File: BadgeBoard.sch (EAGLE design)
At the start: 15 parts

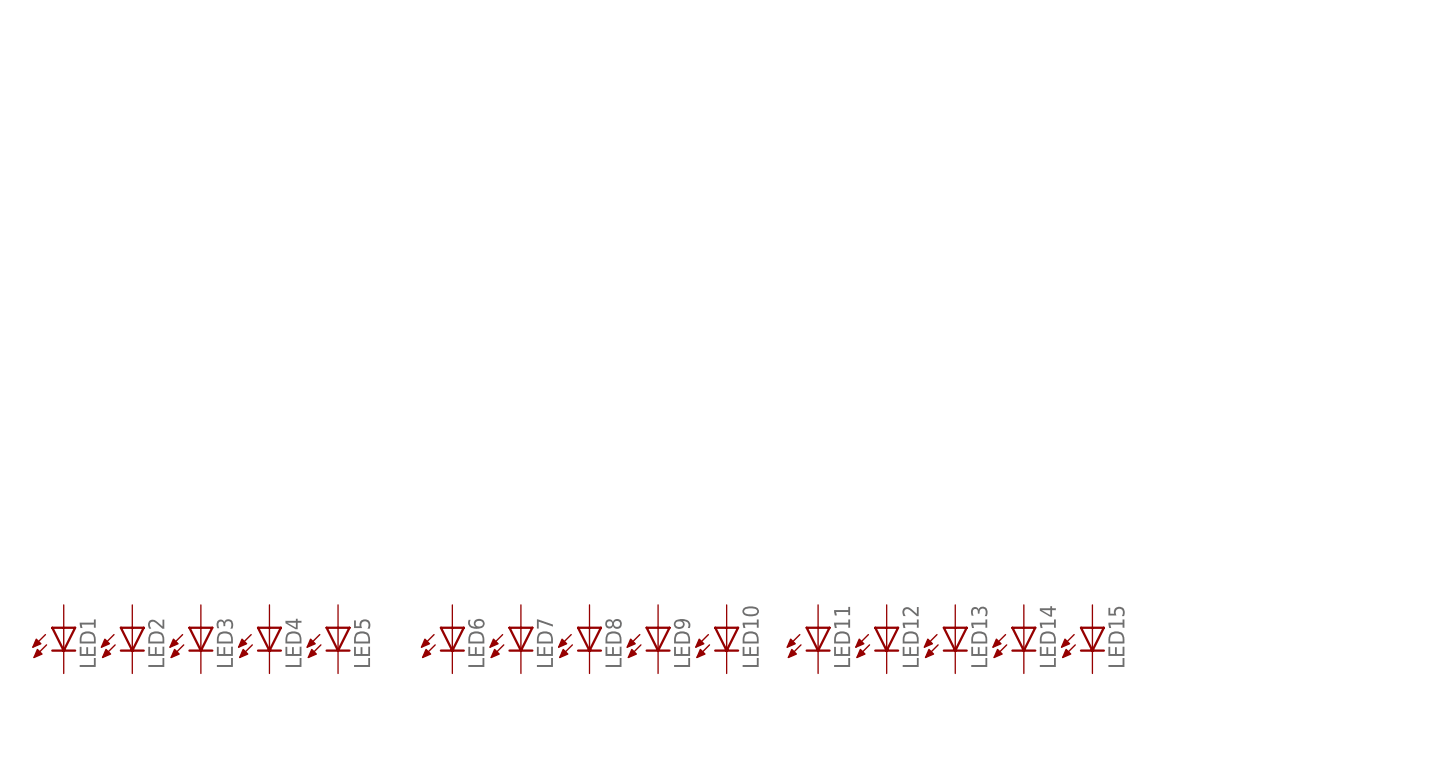
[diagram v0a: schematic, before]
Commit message: update led matrix
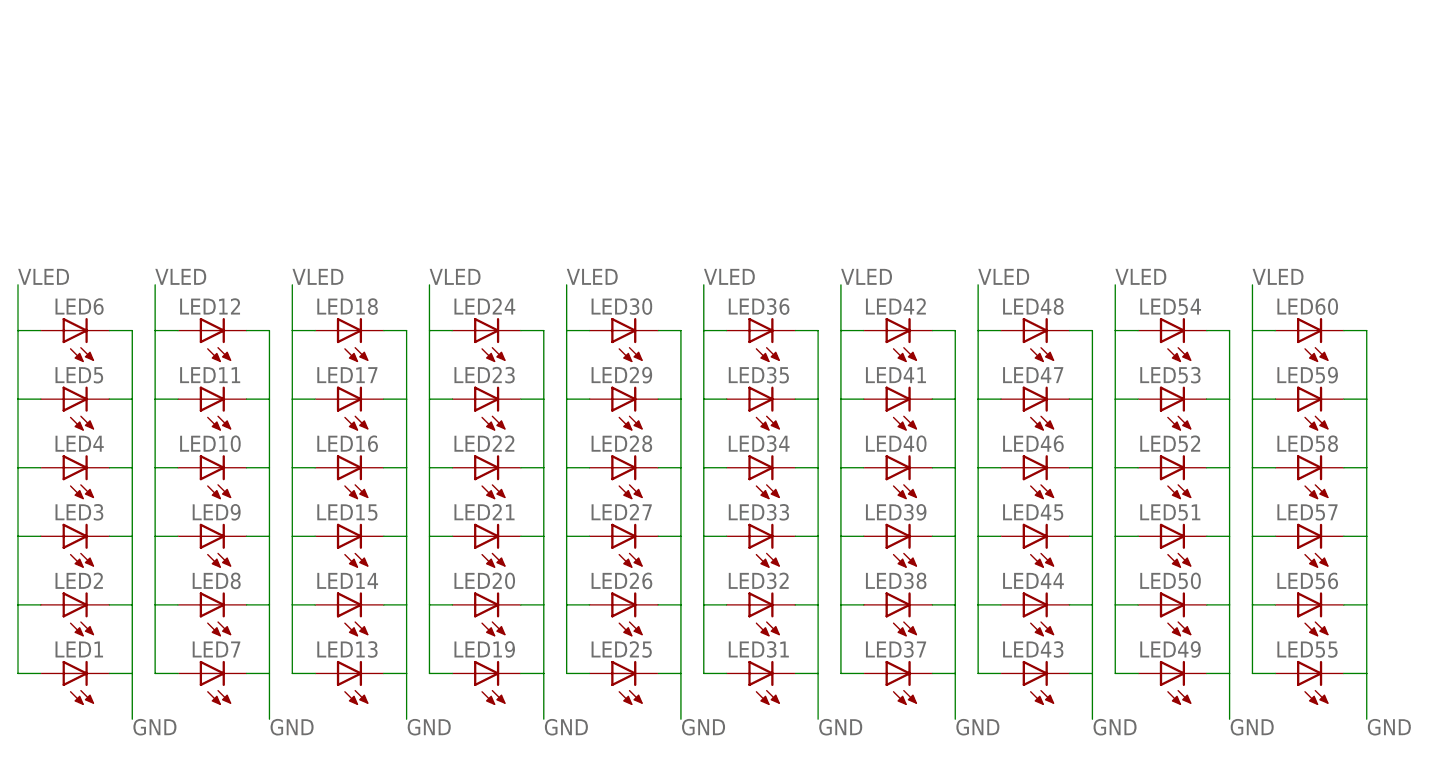
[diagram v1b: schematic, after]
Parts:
- added LED16, LED17, LED18, LED19, LED20, LED21, LED22, LED23, LED24, LED25, LED26, LED27, LED28, LED29, LED30, LED31, LED32, LED33, LED34, LED35, LED36, LED37, LED38, LED39, LED40, LED41, LED42, LED43, LED44, LED45, LED46, LED47, LED48, LED49, LED50, LED51, LED52, LED53, LED54, LED55, LED56, LED57, LED58, LED59, LED60: (no value), adafruit:LED3MM
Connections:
- new net GND: LED10.C, LED11.C, LED12.C, LED7.C, LED8.C, LED9.C
- new net VLED: LED10.A, LED11.A, LED12.A, LED7.A, LED8.A, LED9.A
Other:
- moved on the sheet: LED1, LED10, LED11, LED12, LED13, LED14, LED15, LED2, LED3, LED4, LED5, LED6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

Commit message: More layout
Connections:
- net GND: now also LED1.C, LED13.C, LED14.C, LED15.C, LED16.C, LED17.C, LED18.C, LED19.C, LED2.C, LED20.C, LED21.C, LED22.C, LED23.C, LED24.C, LED25.C, LED26.C, LED27.C, LED28.C, LED29.C, LED3.C, LED30.C, LED31.C, LED32.C, LED33.C, LED34.C, LED35.C, LED36.C, LED37.C, LED38.C, LED39.C, LED4.C, LED40.C, LED41.C, LED42.C, LED43.C, LED44.C, LED45.C, LED46.C, LED47.C, LED48.C, LED49.C, LED5.C, LED50.C, LED51.C, LED52.C, LED53.C, LED54.C, LED55.C, LED56.C, LED57.C, LED58.C, LED59.C, LED6.C, LED60.C
- net VLED: now also LED1.A, LED13.A, LED14.A, LED15.A, LED16.A, LED17.A, LED18.A, LED19.A, LED2.A, LED20.A, LED21.A, LED22.A, LED23.A, LED24.A, LED25.A, LED26.A, LED27.A, LED28.A, LED29.A, LED3.A, LED30.A, LED31.A, LED32.A, LED33.A, LED34.A, LED35.A, LED36.A, LED37.A, LED38.A, LED39.A, LED4.A, LED40.A, LED41.A, LED42.A, LED43.A, LED44.A, LED45.A, LED46.A, LED47.A, LED48.A, LED49.A, LED5.A, LED50.A, LED51.A, LED52.A, LED53.A, LED54.A, LED55.A, LED56.A, LED57.A, LED58.A, LED59.A, LED6.A, LED60.A
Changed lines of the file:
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@@
 <setting verticaltext="up"/>
 </settings>
-<grid distance="0.1" unitdist="inch" unit="inch" style="lines" multiple="1" display="yes" altdistance="0.01" altunitdist="inch" altunit="inch"/>
+<grid distance="0.1" unitdist="inch" unit="inch" style="lines" multiple="1" display="no" altdistance="0.01" altunitdist="inch" altunit="inch"/>
 <layers>
 <layer number="1" name="Top" color="4" fill="1" visible="no" active="no"/>
@@
 <wire x1="2.54" y1="20.32" x2="5.08" y2="20.32" width="0.1524" layer="91"/>
 <wire x1="2.54" y1="12.7" x2="5.08" y2="12.7" width="0.1524" layer="91"/>
+<pinref part="LED6" gate="G$1" pin="A"/>
+<pinref part="LED5" gate="G$1" pin="A"/>
+<pinref part="LED4" gate="G$1" pin="A"/>
+<pinref part="LED3" gate="G$1" pin="A"/>
+<pinref part="LED2" gate="G$1" pin="A"/>
+<pinref part="LED1" gate="G$1" pin="A"/>
 </segment>
 <segment>
@@
 <wire x1="33.02" y1="20.32" x2="35.56" y2="20.32" width="0.1524" layer="91"/>
 <wire x1="33.02" y1="12.7" x2="35.56" y2="12.7" width="0.1524" layer="91"/>
+<pinref part="LED18" gate="G$1" pin="A"/>
+<pinref part="LED17" gate="G$1" pin="A"/>
+<pinref part="LED16" gate="G$1" pin="A"/>
+<pinref part="LED15" gate="G$1" pin="A"/>
+<pinref part="LED14" gate="G$1" pin="A"/>
+<pinref part="LED13" gate="G$1" pin="A"/>
 </segment>
 <segment>
@@
 <wire x1="48.26" y1="20.32" x2="50.8" y2="20.32" width="0.1524" layer="91"/>
 <wire x1="48.26" y1="12.7" x2="50.8" y2="12.7" width="0.1524" layer="91"/>
+<pinref part="LED19" gate="G$1" pin="A"/>
+<pinref part="LED20" gate="G$1" pin="A"/>
+<pinref part="LED21" gate="G$1" pin="A"/>
+<pinref part="LED22" gate="G$1" pin="A"/>
+<pinref part="LED23" gate="G$1" pin="A"/>
+<pinref part="LED24" gate="G$1" pin="A"/>
 </segment>
 <segment>
@@
 <wire x1="63.5" y1="20.32" x2="66.04" y2="20.32" width="0.1524" layer="91"/>
 <wire x1="63.5" y1="12.7" x2="66.04" y2="12.7" width="0.1524" layer="91"/>
+<pinref part="LED30" gate="G$1" pin="A"/>
+<pinref part="LED29" gate="G$1" pin="A"/>
+<pinref part="LED28" gate="G$1" pin="A"/>
+<pinref part="LED27" gate="G$1" pin="A"/>
+<pinref part="LED26" gate="G$1" pin="A"/>
+<pinref part="LED25" gate="G$1" pin="A"/>
 </segment>
 <segment>
@@
 <wire x1="78.74" y1="20.32" x2="81.28" y2="20.32" width="0.1524" layer="91"/>
 <wire x1="78.74" y1="12.7" x2="81.28" y2="12.7" width="0.1524" layer="91"/>
+<pinref part="LED31" gate="G$1" pin="A"/>
+<pinref part="LED32" gate="G$1" pin="A"/>
+<pinref part="LED33" gate="G$1" pin="A"/>
+<pinref part="LED34" gate="G$1" pin="A"/>
+<pinref part="LED35" gate="G$1" pin="A"/>
+<pinref part="LED36" gate="G$1" pin="A"/>
 </segment>
 <segment>
@@
 <wire x1="109.22" y1="20.32" x2="111.76" y2="20.32" width="0.1524" layer="91"/>
 <wire x1="109.22" y1="12.7" x2="111.76" y2="12.7" width="0.1524" layer="91"/>
+<pinref part="LED43" gate="G$1" pin="A"/>
+<pinref part="LED44" gate="G$1" pin="A"/>
+<pinref part="LED45" gate="G$1" pin="A"/>
+<pinref part="LED46" gate="G$1" pin="A"/>
+<pinref part="LED47" gate="G$1" pin="A"/>
+<pinref part="LED48" gate="G$1" pin="A"/>
 </segment>
 <segment>
@@
 <wire x1="93.98" y1="20.32" x2="96.52" y2="20.32" width="0.1524" layer="91"/>
 <wire x1="93.98" y1="12.7" x2="96.52" y2="12.7" width="0.1524" layer="91"/>
+<pinref part="LED42" gate="G$1" pin="A"/>
+<pinref part="LED41" gate="G$1" pin="A"/>
+<pinref part="LED40" gate="G$1" pin="A"/>
+<pinref part="LED39" gate="G$1" pin="A"/>
+<pinref part="LED38" gate="G$1" pin="A"/>
+<pinref part="LED37" gate="G$1" pin="A"/>
 </segment>
 <segment>
@@
 <wire x1="124.46" y1="20.32" x2="127" y2="20.32" width="0.1524" layer="91"/>
 <wire x1="124.46" y1="12.7" x2="127" y2="12.7" width="0.1524" layer="91"/>
+<pinref part="LED54" gate="G$1" pin="A"/>
+<pinref part="LED53" gate="G$1" pin="A"/>
+<pinref part="LED52" gate="G$1" pin="A"/>
+<pinref part="LED51" gate="G$1" pin="A"/>
+<pinref part="LED50" gate="G$1" pin="A"/>
+<pinref part="LED49" gate="G$1" pin="A"/>
 </segment>
 <segment>
@@
 <wire x1="139.7" y1="20.32" x2="142.24" y2="20.32" width="0.1524" layer="91"/>
 <wire x1="139.7" y1="12.7" x2="142.24" y2="12.7" width="0.1524" layer="91"/>
+<pinref part="LED55" gate="G$1" pin="A"/>
+<pinref part="LED56" gate="G$1" pin="A"/>
+<pinref part="LED57" gate="G$1" pin="A"/>
+<pinref part="LED58" gate="G$1" pin="A"/>
+<pinref part="LED59" gate="G$1" pin="A"/>
+<pinref part="LED60" gate="G$1" pin="A"/>
 </segment>
 </net>
@@
 <wire x1="12.7" y1="12.7" x2="15.24" y2="12.7" width="0.1524" layer="91"/>
 <wire x1="12.7" y1="20.32" x2="15.24" y2="20.32" width="0.1524" layer="91"/>
+<pinref part="LED6" gate="G$1" pin="C"/>
+<pinref part="LED5" gate="G$1" pin="C"/>
+<pinref part="LED4" gate="G$1" pin="C"/>
+<pinref part="LED3" gate="G$1" pin="C"/>
+<pinref part="LED2" gate="G$1" pin="C"/>
+<pinref part="LED1" gate="G$1" pin="C"/>
 </segment>
 <segment>
@@
 <wire x1="43.18" y1="12.7" x2="45.72" y2="12.7" width="0.1524" layer="91"/>
 <wire x1="43.18" y1="20.32" x2="45.72" y2="20.32" width="0.1524" layer="91"/>
+<pinref part="LED18" gate="G$1" pin="C"/>
+<pinref part="LED17" gate="G$1" pin="C"/>
+<pinref part="LED16" gate="G$1" pin="C"/>
+<pinref part="LED15" gate="G$1" pin="C"/>
+<pinref part="LED14" gate="G$1" pin="C"/>
+<pinref part="LED13" gate="G$1" pin="C"/>
 </segment>
 <segment>
@@
 <wire x1="149.86" y1="12.7" x2="152.4" y2="12.7" width="0.1524" layer="91"/>
 <wire x1="149.86" y1="20.32" x2="152.4" y2="20.32" width="0.1524" layer="91"/>
+<pinref part="LED55" gate="G$1" pin="C"/>
+<pinref part="LED56" gate="G$1" pin="C"/>
+<pinref part="LED57" gate="G$1" pin="C"/>
+<pinref part="LED58" gate="G$1" pin="C"/>
+<pinref part="LED59" gate="G$1" pin="C"/>
+<pinref part="LED60" gate="G$1" pin="C"/>
 </segment>
 <segment>
@@
 <wire x1="134.62" y1="12.7" x2="137.16" y2="12.7" width="0.1524" layer="91"/>
 <wire x1="134.62" y1="20.32" x2="137.16" y2="20.32" width="0.1524" layer="91"/>
+<pinref part="LED54" gate="G$1" pin="C"/>
+<pinref part="LED53" gate="G$1" pin="C"/>
+<pinref part="LED52" gate="G$1" pin="C"/>
+<pinref part="LED51" gate="G$1" pin="C"/>
+<pinref part="LED50" gate="G$1" pin="C"/>
+<pinref part="LED49" gate="G$1" pin="C"/>
 </segment>
 <segment>
@@
 <wire x1="119.38" y1="12.7" x2="121.92" y2="12.7" width="0.1524" layer="91"/>
 <wire x1="119.38" y1="20.32" x2="121.92" y2="20.32" width="0.1524" layer="91"/>
+<pinref part="LED43" gate="G$1" pin="C"/>
+<pinref part="LED44" gate="G$1" pin="C"/>
+<pinref part="LED45" gate="G$1" pin="C"/>
+<pinref part="LED46" gate="G$1" pin="C"/>
+<pinref part="LED47" gate="G$1" pin="C"/>
+<pinref part="LED48" gate="G$1" pin="C"/>
 </segment>
 <segment>
@@
 <wire x1="104.14" y1="12.7" x2="106.68" y2="12.7" width="0.1524" layer="91"/>
 <wire x1="104.14" y1="20.32" x2="106.68" y2="20.32" width="0.1524" layer="91"/>
+<pinref part="LED42" gate="G$1" pin="C"/>
+<pinref part="LED41" gate="G$1" pin="C"/>
+<pinref part="LED40" gate="G$1" pin="C"/>
+<pinref part="LED39" gate="G$1" pin="C"/>
+<pinref part="LED38" gate="G$1" pin="C"/>
+<pinref part="LED37" gate="G$1" pin="C"/>
 </segment>
 <segment>
@@
 <wire x1="88.9" y1="12.7" x2="91.44" y2="12.7" width="0.1524" layer="91"/>
 <wire x1="88.9" y1="20.32" x2="91.44" y2="20.32" width="0.1524" layer="91"/>
+<pinref part="LED31" gate="G$1" pin="C"/>
+<pinref part="LED32" gate="G$1" pin="C"/>
+<pinref part="LED33" gate="G$1" pin="C"/>
+<pinref part="LED34" gate="G$1" pin="C"/>
+<pinref part="LED35" gate="G$1" pin="C"/>
+<pinref part="LED36" gate="G$1" pin="C"/>
 </segment>
 <segment>
@@
 <wire x1="58.42" y1="12.7" x2="60.96" y2="12.7" width="0.1524" layer="91"/>
 <wire x1="58.42" y1="20.32" x2="60.96" y2="20.32" width="0.1524" layer="91"/>
+<pinref part="LED19" gate="G$1" pin="C"/>
+<pinref part="LED20" gate="G$1" pin="C"/>
+<pinref part="LED21" gate="G$1" pin="C"/>
+<pinref part="LED22" gate="G$1" pin="C"/>
+<pinref part="LED23" gate="G$1" pin="C"/>
+<pinref part="LED24" gate="G$1" pin="C"/>
 </segment>
 <segment>
@@
 <wire x1="73.66" y1="12.7" x2="76.2" y2="12.7" width="0.1524" layer="91"/>
 <wire x1="73.66" y1="20.32" x2="76.2" y2="20.32" width="0.1524" layer="91"/>
+<pinref part="LED30" gate="G$1" pin="C"/>
+<pinref part="LED29" gate="G$1" pin="C"/>
+<pinref part="LED28" gate="G$1" pin="C"/>
+<pinref part="LED27" gate="G$1" pin="C"/>
+<pinref part="LED26" gate="G$1" pin="C"/>
+<pinref part="LED25" gate="G$1" pin="C"/>
 </segment>
 </net>

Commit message: add switch and i-lim res
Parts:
- added JP1: JUMPER-PAD-2-NO, SparkFun-Passives:JUMPER-PAD-2-NO
- added R1: (no value), adafruit:R-US_0207/9
- added U$4: JS202011CQN, switch:JS202011CQN
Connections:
- new net SW_BATT: JP1.1, R1.1, U$4.2
- new net VBATT: U$4.3
- net VLED: now also JP1.2, R1.2
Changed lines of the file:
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@@
 <setting verticaltext="up"/>
 </settings>
-<grid distance="0.1" unitdist="inch" unit="inch" style="lines" multiple="1" display="no" altdistance="0.01" altunitdist="inch" altunit="inch"/>
+<grid distance="0.1" unitdist="inch" unit="inch" style="lines" multiple="1" display="yes" altdistance="0.01" altunitdist="inch" altunit="inch"/>
 <layers>
 <layer number="1" name="Top" color="4" fill="1" visible="no" active="no"/>
@@
 <part name="LED59" library="adafruit" deviceset="LED" device="3MM"/>
 <part name="LED60" library="adafruit" deviceset="LED" device="3MM"/>
+<part name="U$4" library="switch" deviceset="JS202011CQN" device=""/>
+<part name="R1" library="adafruit" deviceset="R-US_" device="0207/9"/>
+<part name="JP1" library="SparkFun-Passives" deviceset="JUMPER-PAD-2-NO" device=""/>
 </parts>
 <sheets>
@@
 <instance part="LED59" gate="G$1" x="144.78" y="35.56" rot="R90"/>
 <instance part="LED60" gate="G$1" x="144.78" y="43.18" rot="R90"/>
+<instance part="U$4" gate="G$1" x="30.48" y="71.12"/>
+<instance part="R1" gate="G$1" x="78.74" y="71.12"/>
+<instance part="JP1" gate="G$1" x="78.74" y="63.5"/>
 </instances>
 <busses>
@@
 <pinref part="LED60" gate="G$1" pin="A"/>
 </segment>
+<segment>
+<wire x1="83.82" y1="71.12" x2="86.36" y2="71.12" width="0.1524" layer="91"/>
+<label x="88.9" y="71.12" size="1.778" layer="95"/>
+<pinref part="R1" gate="G$1" pin="2"/>
+<wire x1="86.36" y1="71.12" x2="88.9" y2="71.12" width="0.1524" layer="91"/>
+<wire x1="86.36" y1="71.12" x2="86.36" y2="63.5" width="0.1524" layer="91"/>
+<pinref part="JP1" gate="G$1" pin="2"/>
+<wire x1="86.36" y1="63.5" x2="83.82" y2="63.5" width="0.1524" layer="91"/>
+<junction x="86.36" y="71.12"/>
+</segment>
 </net>
 <net name="GND" class="0">
@@
 </segment>
 </net>
+<net name="SW_BATT" class="0">
+<segment>
+<pinref part="U$4" gate="G$1" pin="2"/>
+<wire x1="20.32" y1="71.12" x2="25.4" y2="71.12" width="0.1524" layer="91"/>
+<label x="20.32" y="71.12" size="1.778" layer="95" rot="MR0"/>
+</segment>
+<segment>
+<wire x1="68.58" y1="71.12" x2="71.12" y2="71.12" width="0.1524" layer="91"/>
+<label x="68.58" y="71.12" size="1.778" layer="95" rot="MR0"/>
+<pinref part="R1" gate="G$1" pin="1"/>
+<wire x1="71.12" y1="71.12" x2="73.66" y2="71.12" width="0.1524" layer="91"/>
+<wire x1="71.12" y1="71.12" x2="71.12" y2="63.5" width="0.1524" layer="91"/>
+<pinref part="JP1" gate="G$1" pin="1"/>
+<wire x1="71.12" y1="63.5" x2="73.66" y2="63.5" width="0.1524" layer="91"/>
+<junction x="71.12" y="71.12"/>
+</segment>
+</net>
+<net name="VBATT" class="0">
+<segment>
+<pinref part="U$4" gate="G$1" pin="3"/>
+<wire x1="20.32" y1="68.58" x2="25.4" y2="68.58" width="0.1524" layer="91"/>
+<label x="20.32" y="68.58" size="1.778" layer="95" rot="MR0"/>
+</segment>
+</net>
